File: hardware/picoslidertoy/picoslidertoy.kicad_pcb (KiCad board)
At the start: 2 copper layers, 165.1 x 76.2 mm, 50 parts, among them SW1 Capacitive Button, SW2 Capacitive Button, SW3 Capacitive Button, SW4 Capacitive Button, SW5 Capacitive Button, SW6 Capacitive Button, SW7 Capacitive Button, SW8 Capacitive Button, SW9 Capacitive Button, U1 Pico

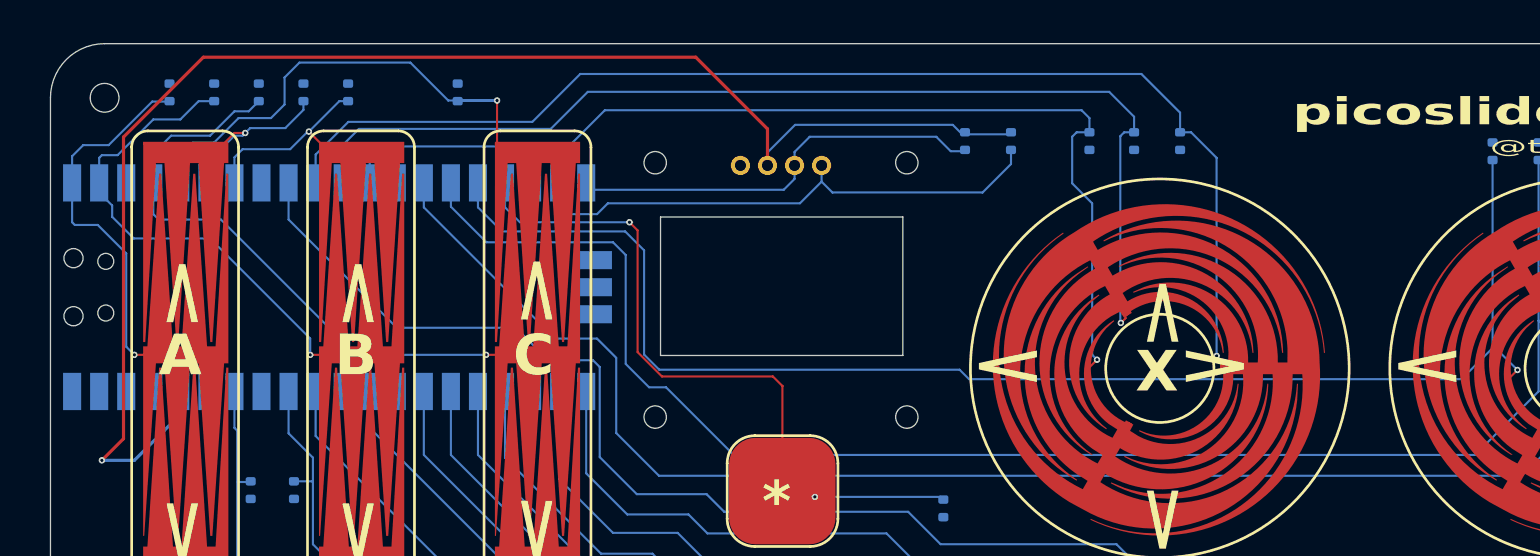
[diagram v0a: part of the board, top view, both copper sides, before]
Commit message: pcb display positioning tune
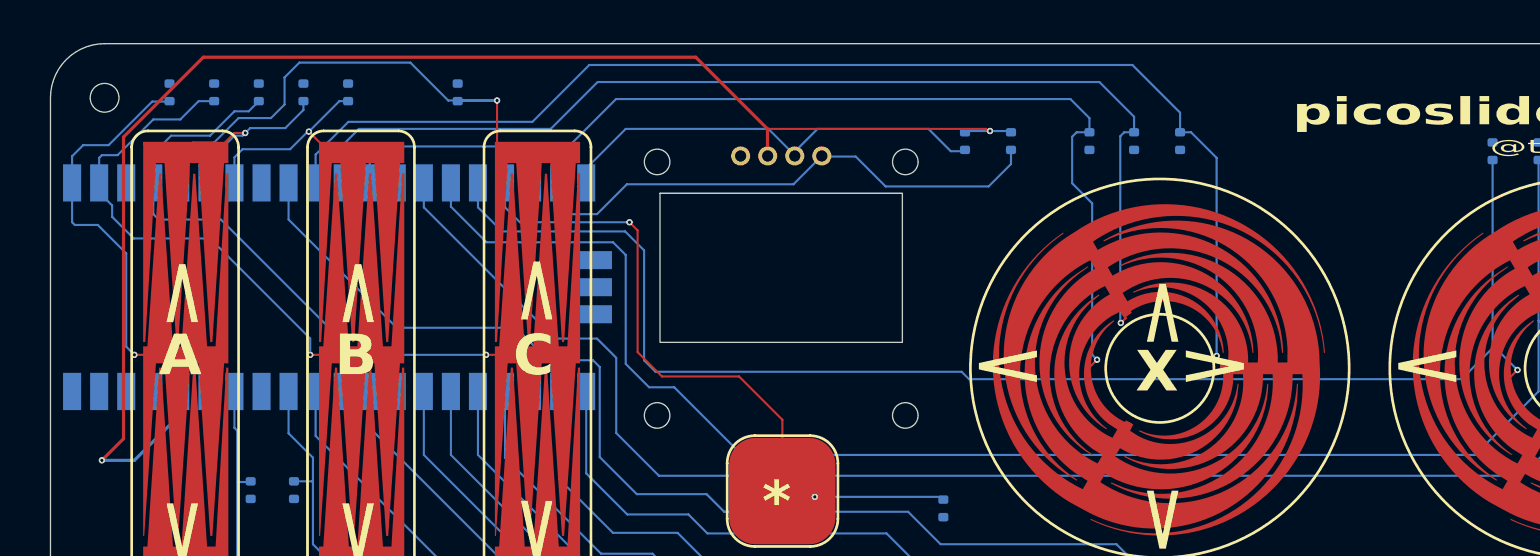
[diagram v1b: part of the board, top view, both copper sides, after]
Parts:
- removed DISP1: HS96L03W2C03, todbot_stuff:OLED-TH_under_L27.8-W27.2-P2.54_C9900033791
- removed H5, H6, H7, H8: MountingHole, MountingHole:MountingHole_2.1mm
- added DISP2: HS96L03W2C03, todbot_stuff:OLED-TH_under_fixed_L27.8-W27.2-P2.54_C9900033791, F.Cu at (94.0, 35.9)
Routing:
- net /SCL: track 39.7 -> 42.1 mm
- net /TPAD9: track 63.4 -> 61.5 mm
- net /ROT1C: track 106.2 -> 107.0 mm
- net /ROT1B: track 103.7 -> 104.5 mm
- net +3V3: track 138.8 -> 138.0 mm, vias 1 -> 2
- net /ROT1A: track 115.8 -> 116.5 mm
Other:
- outline, holes or cut-outs redrawn

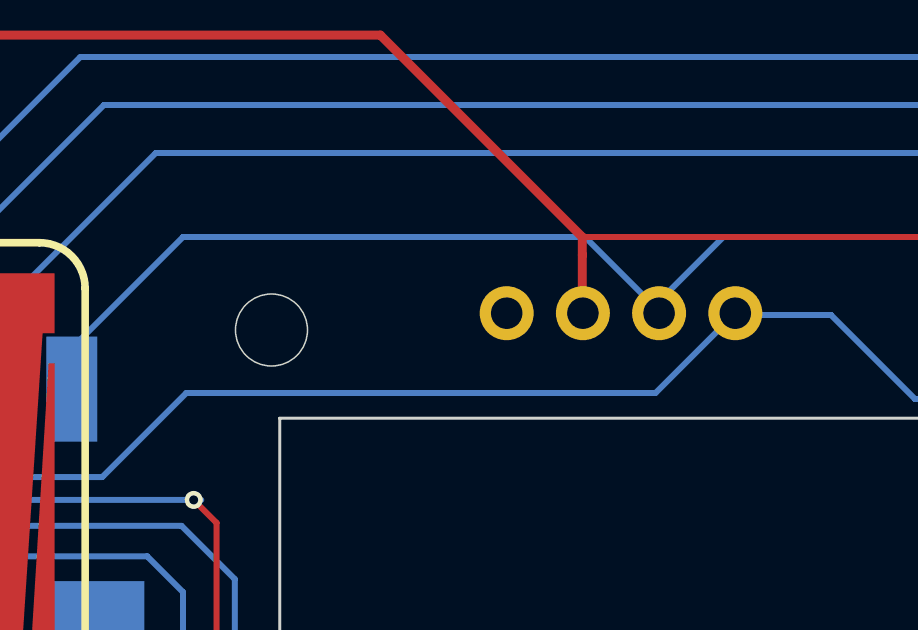
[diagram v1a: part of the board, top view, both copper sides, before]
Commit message: pcb display position tuning
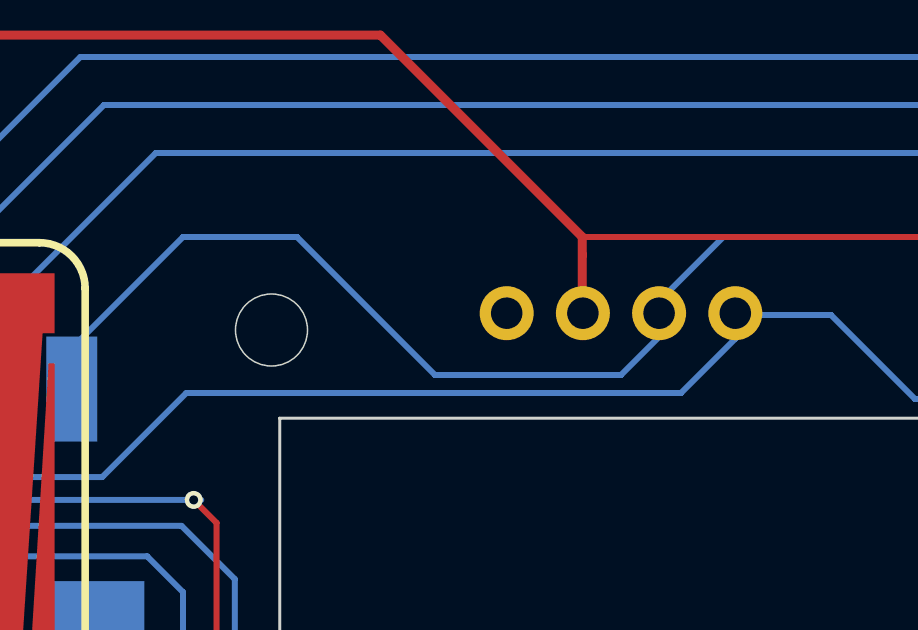
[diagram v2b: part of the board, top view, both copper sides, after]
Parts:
- renumbered DISP2 to DISP1
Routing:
- net /SCL: track 42.1 -> 44.2 mm
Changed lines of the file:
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@@
 		(layer "F.Cu")
 		(at 94 35.94)
-		(property "Reference" "DISP2"
-			(at 8.2 1.86 0)
+		(property "Reference" "DISP1"
+			(at -7.6 -0.34 0)
 			(layer "B.SilkS")
 			(effects
@@
 					(thickness 0.15)
 				)
+				(justify mirror)
 			)
 		)
@@
 	)
 	(segment
-		(start 92.8 33.4)
-		(end 79.4 33.4)
+		(start 94 38)
+		(end 87.8 38)
 		(width 0.2)
 		(layer "B.Cu")
@@
 	)
 	(segment
-		(start 79.4 33.4)
-		(end 75.692 37.108)
+		(start 87.8 38)
+		(end 83.2 33.4)
 		(width 0.2)
 		(layer "B.Cu")
@@
 	)
 	(segment
-		(start 95.27 35.94)
-		(end 95.27 35.87)
+		(start 109.918 35.496)
+		(end 107.822 33.4)
 		(width 0.2)
 		(layer "B.Cu")
@@
 	)
 	(segment
-		(start 109.918 35.496)
-		(end 107.822 33.4)
+		(start 111.125 35.496)
+		(end 109.918 35.496)
 		(width 0.2)
 		(layer "B.Cu")
@@
 	)
 	(segment
-		(start 111.125 35.496)
-		(end 109.918 35.496)
+		(start 83.2 33.4)
+		(end 79.4 33.4)
+		(width 0.2)
+		(layer "B.Cu")
+		(net 9)
+	)
+	(segment
+		(start 95.27 35.94)
+		(end 95.27 36.73)
 		(width 0.2)
 		(layer "B.Cu")
@@
 	)
 	(segment
-		(start 75.692 37.108)
-		(end 75.692 39.37)
+		(start 95.27 36.73)
+		(end 94 38)
+		(width 0.2)
+		(layer "B.Cu")
+		(net 9)
+	)
+	(segment
+		(start 79.4 33.4)
+		(end 75.692 37.108)
 		(width 0.2)
 		(layer "B.Cu")
@@
 	)
 	(segment
-		(start 95.27 35.87)
-		(end 92.8 33.4)
+		(start 75.692 37.108)
+		(end 75.692 39.37)
 		(width 0.2)
 		(layer "B.Cu")
@@
 	)
 	(segment
-		(start 73.914 41.402)
-		(end 76.708 41.402)
+		(start 96 38.6)
+		(end 97.81 36.79)
+		(width 0.2)
+		(layer "B.Cu")
+		(net 10)
+	)
+	(segment
+		(start 76.708 41.402)
+		(end 79.51 38.6)
 		(width 0.2)
 		(layer "B.Cu")
@@
 	)
 	(segment
-		(start 76.708 41.402)
-		(end 79.51 38.6)
+		(start 97.81 36.79)
+		(end 97.81 35.94)
 		(width 0.2)
 		(layer "B.Cu")
@@
 	)
 	(segment
-		(start 73.152 40.64)
-		(end 73.914 41.402)
+		(start 79.51 38.6)
+		(end 96 38.6)
 		(width 0.2)
 		(layer "B.Cu")
@@
 	)
 	(segment
-		(start 79.51 38.6)
-		(end 95.15 38.6)
+		(start 73.914 41.402)
+		(end 76.708 41.402)
 		(width 0.2)
 		(layer "B.Cu")
@@
 	)
 	(segment
-		(start 95.15 38.6)
-		(end 97.81 35.94)
+		(start 73.152 40.64)
+		(end 73.914 41.402)
 		(width 0.2)
 		(layer "B.Cu")
